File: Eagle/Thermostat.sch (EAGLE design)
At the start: 58 parts, among them J2 USB-MINIB-5PIN, K1 AQY282EHA, K2 AQY282EHA, K3 AQY282EHA, K4 AQY282EHA, K5 AQY282EHA, Q1 MOSFET-PCHANNELSMD

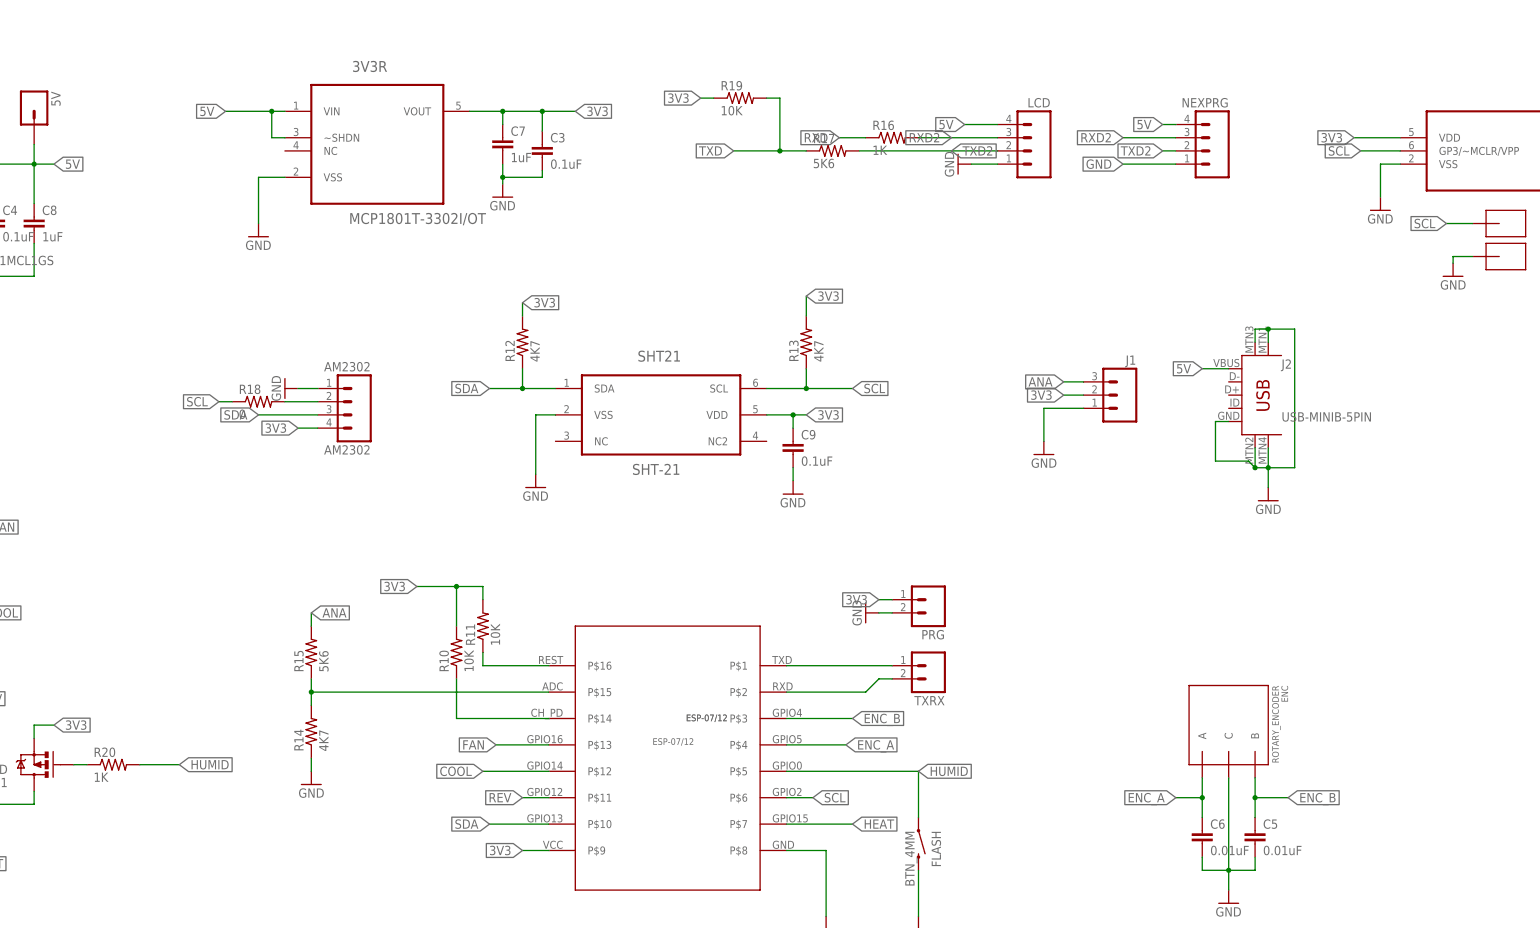
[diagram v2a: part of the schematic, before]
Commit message: Mislabeled MCP1755 as MCP1801
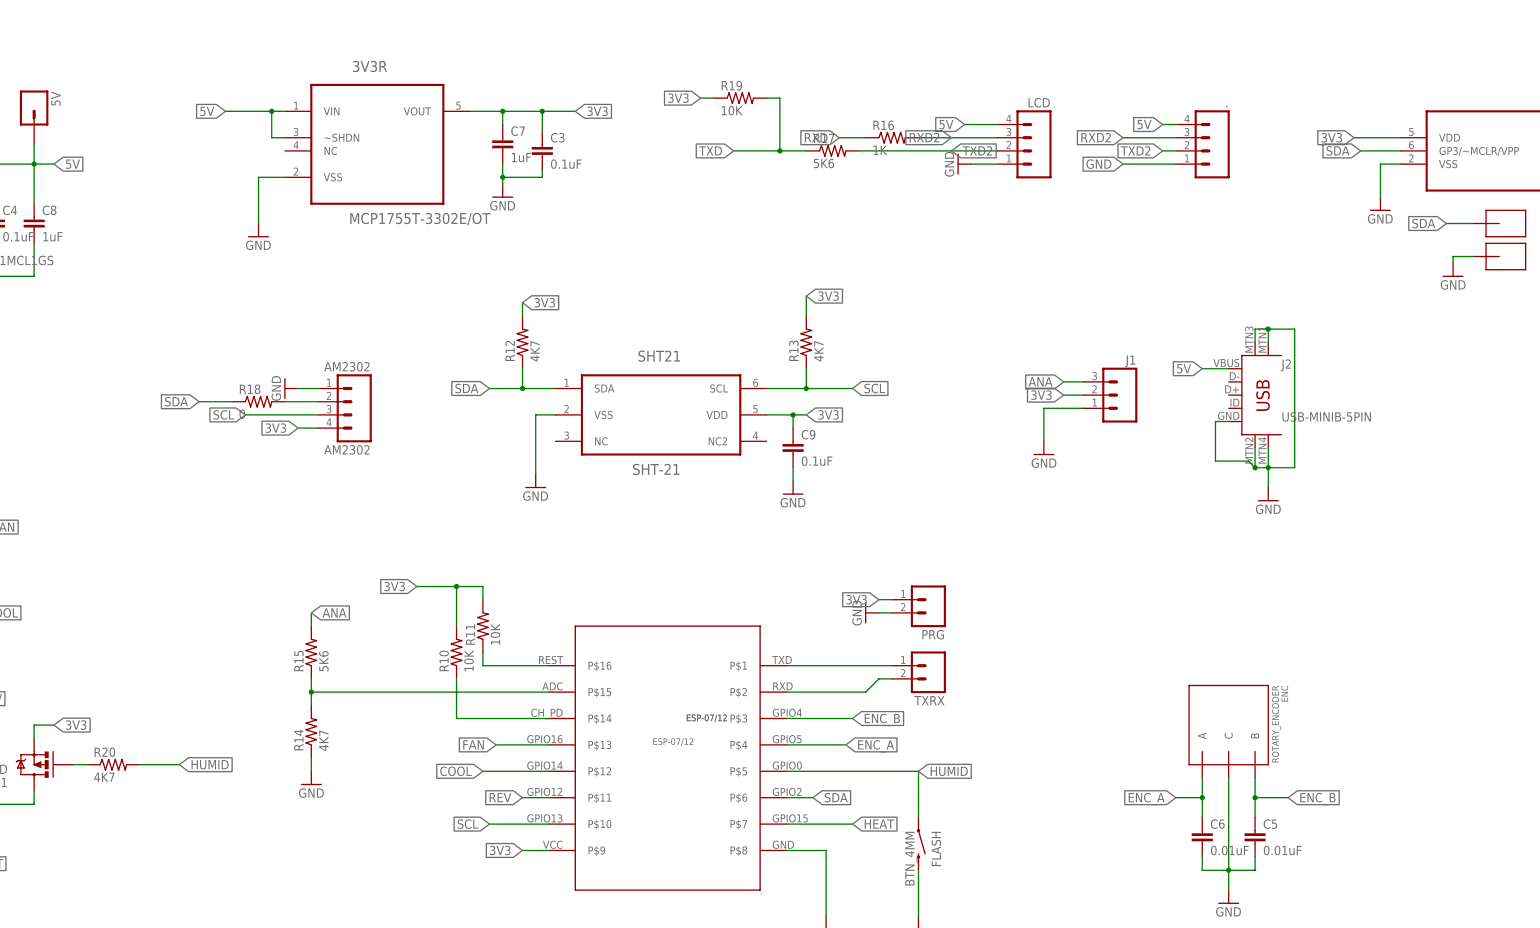
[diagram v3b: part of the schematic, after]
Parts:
- 3V3R: value MCP1801T-3302I/OT -> MCP1755T-3302E/OT
- R20: value 1K -> 4K7
- renumbered NEXPRG to .
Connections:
- net SCL: now also AM2302.3, U$1.P$10; no longer 10F.GP3/~MCLR/VPP, R18.1, U$1.P$6, U$5.P$1
- net SDA: now also 10F.GP3/~MCLR/VPP, R18.1, U$1.P$6, U$5.P$1; no longer AM2302.3, U$1.P$10
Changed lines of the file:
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@@
 <?xml version="1.0" encoding="utf-8"?>
 <!DOCTYPE eagle SYSTEM "eagle.dtd">
-<eagle version="7.5.0">
+<eagle version="7.6.0">
 <drawing>
 <settings>
@@
 <part name="GND23" library="supply1" deviceset="GND" device=""/>
 <part name="C3" library="SparkFun-Capacitors" deviceset="CAP" device="0805" value="0.1uF"/>
-<part name="3V3R" library="Microchip_By_element14_Batch_1" deviceset="MCP1801T-3302I/OT" device=""/>
+<part name="3V3R" library="Microchip_By_element14_Batch_1" deviceset="MCP1801T-3302I/OT" device="" value="MCP1755T-3302E/OT"/>
 <part name="R17" library="SparkFun-Resistors" deviceset="RESISTOR" device="0805-RES" value="5K6"/>
 <part name="10F" library="Microchip_By_element14_Batch_1" deviceset="PIC10F202T-I/OT" device=""/>
@@
 <part name="R12" library="SparkFun-Resistors" deviceset="RESISTOR" device="0805-RES" value="4K7"/>
 <part name="R13" library="SparkFun-Resistors" deviceset="RESISTOR" device="0805-RES" value="4K7"/>
-<part name="NEXPRG" library="SparkFun-Connectors" deviceset="M04" device="PTH"/>
+<part name="." library="SparkFun-Connectors" deviceset="M04" device="PTH"/>
 <part name="GND17" library="supply1" deviceset="GND" device=""/>
 <part name="U$2" library="CuriousTech" deviceset="SMD-PAD1" device=""/>
@@
 <part name="GND29" library="supply1" deviceset="GND" device=""/>
 <part name="R19" library="SparkFun-Resistors" deviceset="RESISTOR" device="0805-RES" value="10K"/>
-<part name="R20" library="SparkFun-Passives" deviceset="RESISTOR" device="0805-RES" value="1K"/>
+<part name="R20" library="SparkFun-Passives" deviceset="RESISTOR" device="0805-RES" value="4K7"/>
 </parts>
 <sheets>
@@
 <instance part="R12" gate="G$1" x="218.44" y="119.38" rot="R90"/>
 <instance part="R13" gate="G$1" x="273.05" y="119.38" rot="R90"/>
-<instance part="NEXPRG" gate="G$1" x="349.25" y="156.21" rot="MR0"/>
+<instance part="." gate="G$1" x="349.25" y="156.21" rot="MR0"/>
 <instance part="GND17" gate="1" x="318.77" y="97.79" rot="MR0"/>
 <instance part="U$2" gate="G$1" x="406.4" y="135.89"/>
@@
 </segment>
 <segment>
-<pinref part="NEXPRG" gate="G$1" pin="1"/>
+<pinref part="." gate="G$1" pin="1"/>
 <wire x1="344.17" y1="153.67" x2="334.01" y2="153.67" width="0.1524" layer="91"/>
 <label x="334.01" y="153.67" size="1.778" layer="95" rot="R180" xref="yes"/>
@@
 </segment>
 <segment>
-<pinref part="NEXPRG" gate="G$1" pin="4"/>
+<pinref part="." gate="G$1" pin="4"/>
 <wire x1="344.17" y1="161.29" x2="341.63" y2="161.29" width="0.1524" layer="91"/>
 <label x="341.63" y="161.29" size="1.778" layer="95" rot="R180" xref="yes"/>
@@
 <wire x1="354.33" y1="114.3" x2="349.25" y2="114.3" width="0.1524" layer="91"/>
 <label x="349.25" y="114.3" size="1.778" layer="95" rot="R180" xref="yes"/>
-</segment>
-</net>
-<net name="SCL" class="0">
-<segment>
-<pinref part="U$1" gate="G$1" pin="P$6"/>
-<wire x1="269.24" y1="31.75" x2="274.32" y2="31.75" width="0.1524" layer="91"/>
-<label x="274.32" y="31.75" size="1.778" layer="95" xref="yes"/>
-</segment>
-<segment>
-<wire x1="265.43" y1="110.49" x2="273.05" y2="110.49" width="0.1524" layer="91"/>
-<pinref part="R13" gate="G$1" pin="1"/>
-<wire x1="273.05" y1="110.49" x2="281.94" y2="110.49" width="0.1524" layer="91"/>
-<wire x1="273.05" y1="114.3" x2="273.05" y2="110.49" width="0.1524" layer="91"/>
-<junction x="273.05" y="110.49"/>
-<label x="281.94" y="110.49" size="1.778" layer="95" xref="yes"/>
-<pinref part="SHT21" gate="G$1" pin="SCL"/>
-</segment>
-<segment>
-<pinref part="10F" gate="A" pin="GP3/~MCLR/VPP"/>
-<wire x1="387.35" y1="156.21" x2="379.73" y2="156.21" width="0.1524" layer="91"/>
-<label x="379.73" y="156.21" size="1.778" layer="95" rot="R180" xref="yes"/>
-</segment>
-<segment>
-<pinref part="U$5" gate="G$1" pin="P$1"/>
-<wire x1="401.32" y1="142.24" x2="396.24" y2="142.24" width="0.1524" layer="91"/>
-<label x="396.24" y="142.24" size="1.778" layer="95" rot="R180" xref="yes"/>
-</segment>
-<segment>
-<pinref part="R18" gate="G$1" pin="1"/>
-<wire x1="162.56" y1="107.95" x2="160.02" y2="107.95" width="0.1524" layer="91"/>
-<label x="160.02" y="107.95" size="1.778" layer="95" rot="R180" xref="yes"/>
-</segment>
-</net>
-<net name="SDA" class="0">
-<segment>
-<pinref part="U$1" gate="G$1" pin="P$10"/>
-<wire x1="223.52" y1="26.67" x2="212.09" y2="26.67" width="0.1524" layer="91"/>
-<label x="212.09" y="26.67" size="1.778" layer="95" rot="R180" xref="yes"/>
-</segment>
-<segment>
-<wire x1="167.64" y1="105.41" x2="179.07" y2="105.41" width="0.1524" layer="91"/>
-<pinref part="AM2302" gate="G$1" pin="3"/>
-<label x="167.64" y="105.41" size="1.778" layer="95" rot="R180" xref="yes"/>
-</segment>
-<segment>
-<wire x1="224.79" y1="110.49" x2="218.44" y2="110.49" width="0.1524" layer="91"/>
-<pinref part="R12" gate="G$1" pin="1"/>
-<wire x1="218.44" y1="110.49" x2="212.09" y2="110.49" width="0.1524" layer="91"/>
-<wire x1="218.44" y1="114.3" x2="218.44" y2="110.49" width="0.1524" layer="91"/>
-<junction x="218.44" y="110.49"/>
-<label x="212.09" y="110.49" size="1.778" layer="95" rot="R180" xref="yes"/>
-<pinref part="SHT21" gate="G$1" pin="SDA"/>
 </segment>
 </net>
@@
 </segment>
 <segment>
-<pinref part="NEXPRG" gate="G$1" pin="2"/>
+<pinref part="." gate="G$1" pin="2"/>
 <wire x1="344.17" y1="156.21" x2="341.63" y2="156.21" width="0.1524" layer="91"/>
 <label x="341.63" y="156.21" size="1.778" layer="95" rot="R180" xref="yes"/>
@@
 </segment>
 <segment>
-<pinref part="NEXPRG" gate="G$1" pin="3"/>
+<pinref part="." gate="G$1" pin="3"/>
 <wire x1="344.17" y1="158.75" x2="334.01" y2="158.75" width="0.1524" layer="91"/>
 <label x="334.01" y="158.75" size="1.778" layer="95" rot="R180" xref="yes"/>
@@
 </segment>
 </net>
+<net name="SCL" class="0">
+<segment>
+<wire x1="265.43" y1="110.49" x2="273.05" y2="110.49" width="0.1524" layer="91"/>
+<pinref part="R13" gate="G$1" pin="1"/>
+<wire x1="273.05" y1="110.49" x2="281.94" y2="110.49" width="0.1524" layer="91"/>
+<wire x1="273.05" y1="114.3" x2="273.05" y2="110.49" width="0.1524" layer="91"/>
+<junction x="273.05" y="110.49"/>
+<label x="281.94" y="110.49" size="1.778" layer="95" xref="yes"/>
+<pinref part="SHT21" gate="G$1" pin="SCL"/>
+</segment>
+<segment>
+<pinref part="AM2302" gate="G$1" pin="3"/>
+<wire x1="179.07" y1="105.41" x2="165.1" y2="105.41" width="0.1524" layer="91"/>
+<label x="165.1" y="105.41" size="1.778" layer="95" rot="R180" xref="yes"/>
+</segment>
+<segment>
+<pinref part="U$1" gate="G$1" pin="P$10"/>
+<wire x1="223.52" y1="26.67" x2="212.09" y2="26.67" width="0.1524" layer="91"/>
+<label x="212.09" y="26.67" size="1.778" layer="95" rot="R180" xref="yes"/>
+</segment>
+</net>
+<net name="SDA" class="0">
+<segment>
+<wire x1="224.79" y1="110.49" x2="218.44" y2="110.49" width="0.1524" layer="91"/>
+<pinref part="R12" gate="G$1" pin="1"/>
+<wire x1="218.44" y1="110.49" x2="212.09" y2="110.49" width="0.1524" layer="91"/>
+<wire x1="218.44" y1="114.3" x2="218.44" y2="110.49" width="0.1524" layer="91"/>
+<junction x="218.44" y="110.49"/>
+<label x="212.09" y="110.49" size="1.778" layer="95" rot="R180" xref="yes"/>
+<pinref part="SHT21" gate="G$1" pin="SDA"/>
+</segment>
+<segment>
+<pinref part="U$5" gate="G$1" pin="P$1"/>
+<wire x1="401.32" y1="142.24" x2="396.24" y2="142.24" width="0.1524" layer="91"/>
+<label x="396.24" y="142.24" size="1.778" layer="95" rot="R180" xref="yes"/>
+</segment>
+<segment>
+<pinref part="10F" gate="A" pin="GP3/~MCLR/VPP"/>
+<wire x1="387.35" y1="156.21" x2="379.73" y2="156.21" width="0.1524" layer="91"/>
+<label x="379.73" y="156.21" size="1.778" layer="95" rot="R180" xref="yes"/>
+</segment>
+<segment>
+<pinref part="R18" gate="G$1" pin="1"/>
+<wire x1="162.56" y1="107.95" x2="156.21" y2="107.95" width="0.1524" layer="91"/>
+<label x="156.21" y="107.95" size="1.778" layer="95" rot="R180" xref="yes"/>
+</segment>
+<segment>
+<pinref part="U$1" gate="G$1" pin="P$6"/>
+<wire x1="269.24" y1="31.75" x2="274.32" y2="31.75" width="0.1524" layer="91"/>
+<label x="274.32" y="31.75" size="1.778" layer="95" xref="yes"/>
+</segment>
+</net>
